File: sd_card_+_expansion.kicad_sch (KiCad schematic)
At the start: 1 part, among them J4 Micro_SD_Card_Det1

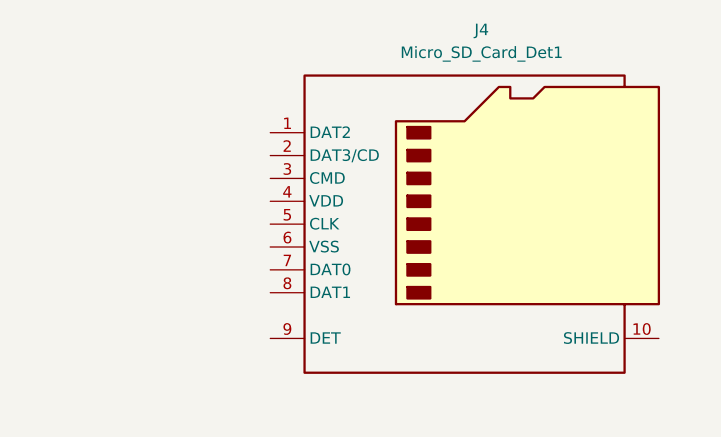
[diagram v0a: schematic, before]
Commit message: Added connectors
Added GPS and SD card connections
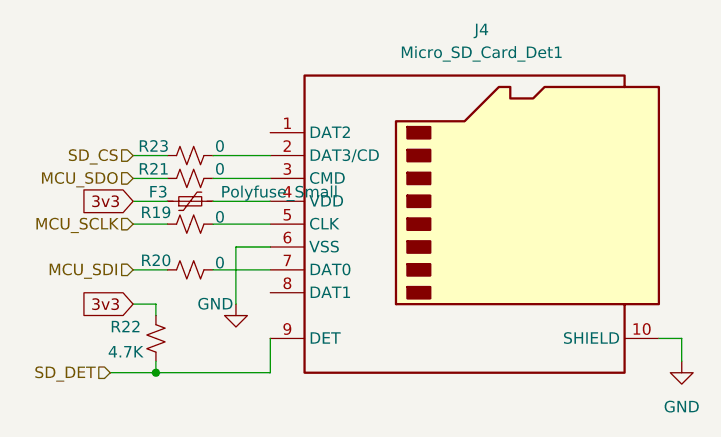
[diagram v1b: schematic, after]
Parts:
- added F3: Polyfuse_Small, symbol Device:Polyfuse_Small
- added R19, R20, R21, R23: 0, symbol Device:R_Small_US
- added R22: 4.7K, symbol Device:R_Small_US
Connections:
- net GND: now reaches J4.10 (SHIELD)
- net GND: now also J4.6 (VSS)
- net at J4.2 (DAT3/CD): now also R23.2
- net at J4.3 (CMD): now also R21.2
- net at J4.4 (VDD): now also F3.2
- net at J4.5 (CLK): now also R19.2
- net at J4.7 (DAT0): now also R20.2
- net SD_DET: now reaches J4.9 (DET)
- net SD_DET: now also R22.2
- new net 3v3: F3.1, R22.1
- new net MCU_SCLK: R19.1
- new net MCU_SDI: R20.1
- new net MCU_SDO: R21.1
- new net SD_CS: R23.1

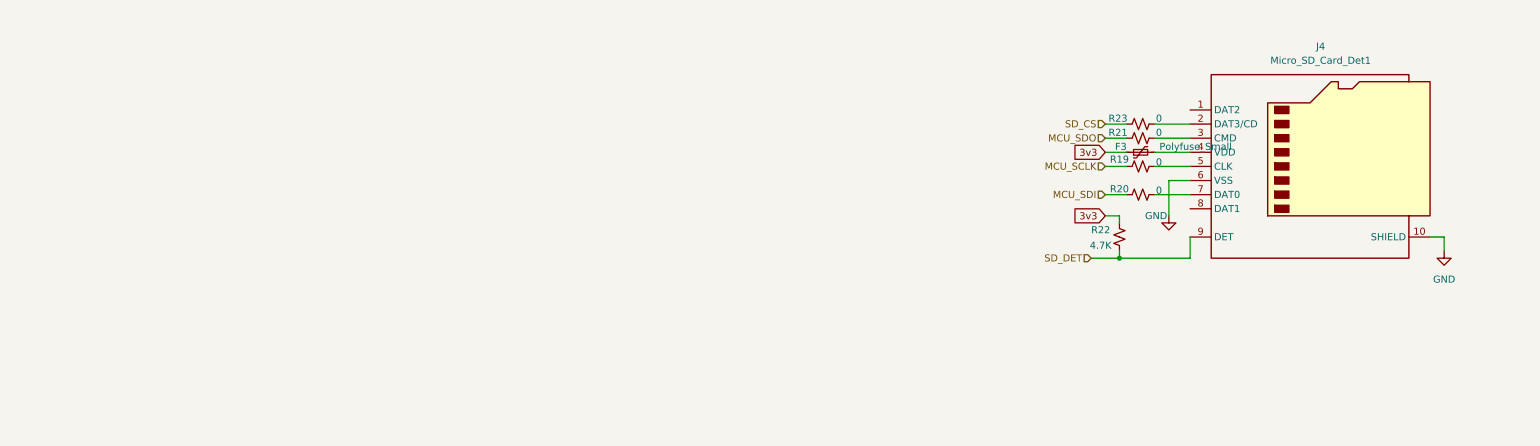
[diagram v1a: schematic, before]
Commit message: Updated schematics
Added the input current sense, expansion header and various test points.
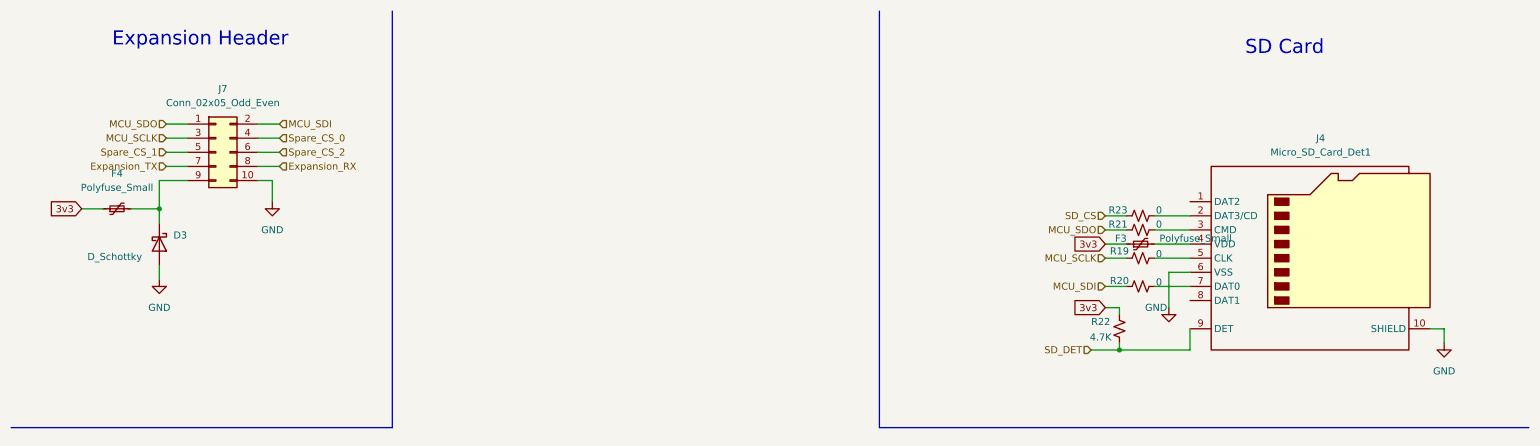
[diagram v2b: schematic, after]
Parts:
- added D3: D_Schottky, symbol Device:D_Schottky
- added F4: Polyfuse_Small, symbol Device:Polyfuse_Small
- added J7: Conn_02x05_Odd_Even, symbol Connector_Generic:Conn_02x05_Odd_Even
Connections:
- net 3v3: now also F4.1
- net GND: now also D3.2 (A), J7.10 (Pin_10)
- net MCU_SCLK: now also J7.3 (Pin_3)
- net MCU_SDI: now also J7.2 (Pin_2)
- net MCU_SDO: now also J7.1 (Pin_1)
- new net: D3.1 (K), F4.2, J7.9 (Pin_9)
- new net Expansion_RX: J7.8 (Pin_8)
- new net Expansion_TX: J7.7 (Pin_7)
- new net Spare_CS_0: J7.4 (Pin_4)
- new net Spare_CS_1: J7.5 (Pin_5)
- new net Spare_CS_2: J7.6 (Pin_6)
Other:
- note added: "Expansion Header"
- note added: "SD Card"
- moved on the sheet: F3, J4, R19, R20, R21, R22, R23

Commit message: Added RPI stuff
Added power passives and usb passives
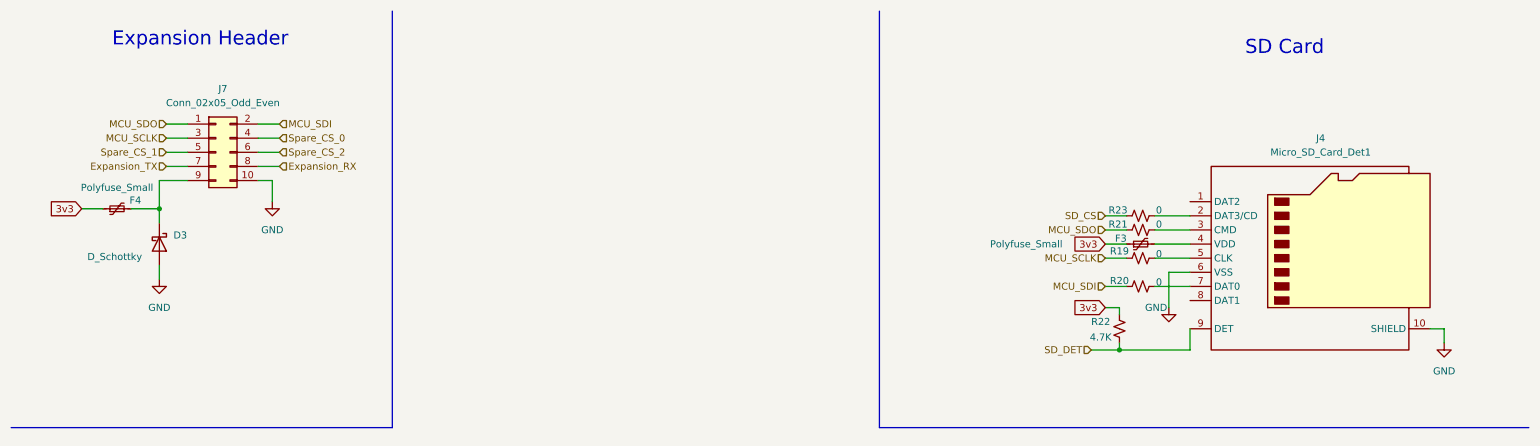
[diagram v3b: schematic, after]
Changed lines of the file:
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@@
 		(on_board yes)
 		(dnp no)
-		(fields_autoplaced yes)
 		(property "Reference" "F4"
-			(at 30.48 41.91 90)
+			(at 33.782 46.736 90)
 			(effects
 				(font
@@
 		)
 		(property "Value" "Polyfuse_Small"
-			(at 224.536 53.594 90)
+			(at 194.056 54.61 90)
 			(effects
 				(font

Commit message: Setup top sheet
Added TVS diodes, updated top sheet, misc label fixes
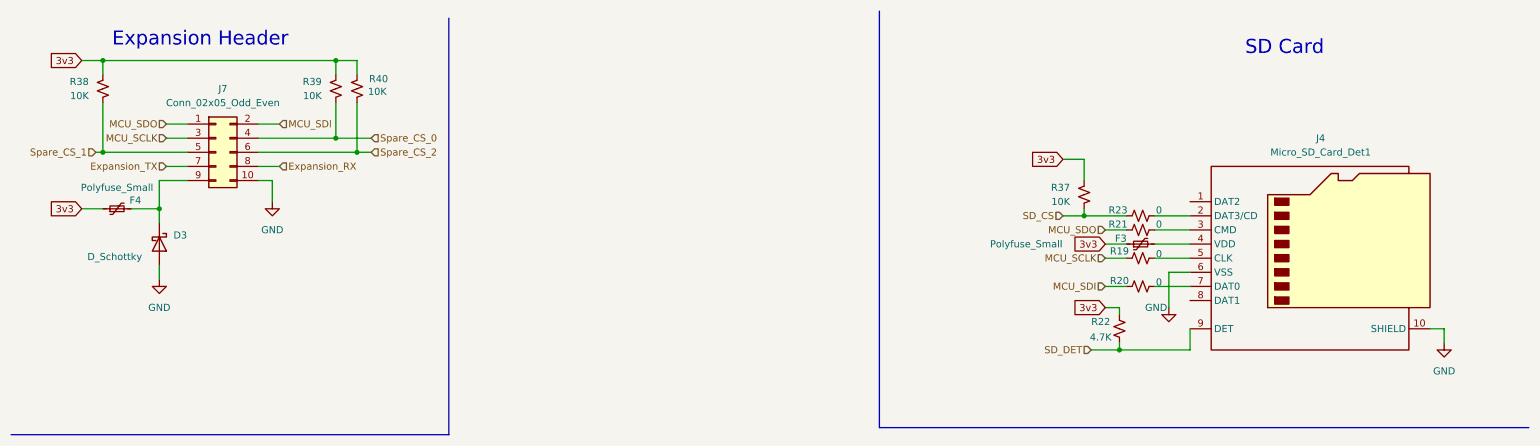
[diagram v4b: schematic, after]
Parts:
- added R37, R38, R39, R40: 10K, symbol Device:R_Small_US
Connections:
- net 3v3: now also R37.1, R38.1, R39.1, R40.1
- net SD_CS: now also R37.2
- net Spare_CS_0: now also R39.2
- net Spare_CS_1: now also R38.2
- net Spare_CS_2: now also R40.2

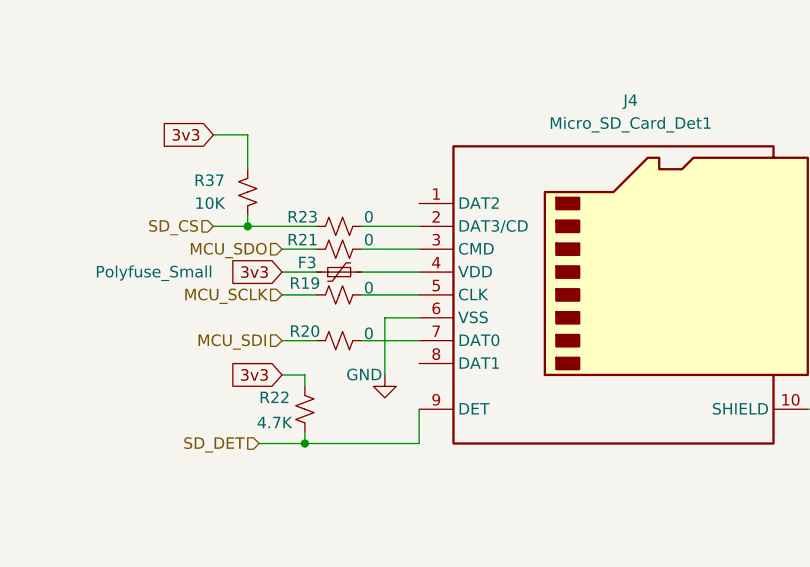
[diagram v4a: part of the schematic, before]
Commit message: Updated sheet to sheet pinout
Updated pinouts and cleared ERCs
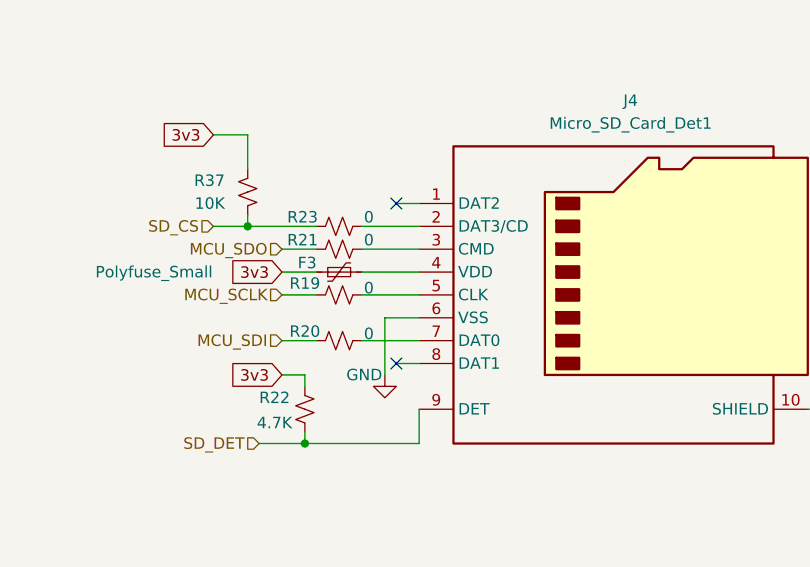
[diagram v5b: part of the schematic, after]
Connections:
- no-connect marks 0 -> 2
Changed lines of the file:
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@@
 		(color 0 0 0 0)
+	)
+	(no_connect
+		(at 220.98 64.77)
+	)
+	(no_connect
+		(at 220.98 46.99)
 	)
 	(wire
 		(pts
 			(xy 208.28 52.07) (xy 212.09 52.07)
+		)
+		(stroke
+			(width 0)
+			(type default)
+		)
+	)
+	(wire
+		(pts
+			(xy 220.98 64.77) (xy 223.52 64.77)
 		)
 		(stroke
@@
 		)
 		(stroke
+			(width 0)
+			(type default)
+		)
+	)
+	(wire
+		(pts
+			(xy 220.98 46.99) (xy 223.52 46.99)
+		)
+		(stroke

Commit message: started layout
Preliminary footprint selection
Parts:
- D3: footprint (none) -> Diode_SMD:D_SOD-123
- F3, F4: footprint (none) -> Fuse:Fuse_1206_3216Metric
- J4: footprint (none) -> Connector_Card:microSD_HC_Hirose_DM3D-SF
- J7: footprint (none) -> Connector_PinHeader_2.54mm:PinHeader_2x05_P2.54mm_Vertical
- R19, R20, R21, R22, R23, R37, R38, R39, R40: footprint (none) -> Resistor_SMD:R_0603_1608Metric
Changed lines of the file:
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@@
 			)
 		)
-		(property "Footprint" ""
+		(property "Footprint" "Connector_Card:microSD_HC_Hirose_DM3D-SF"
 			(at 298.45 39.37 0)
 			(effects
@@
 			)
 		)
-		(property "Footprint" ""
+		(property "Footprint" "Resistor_SMD:R_0603_1608Metric"
 			(at 210.82 69.85 0)
 			(effects
@@
 			)
 		)
-		(property "Footprint" ""
+		(property "Footprint" "Resistor_SMD:R_0603_1608Metric"
 			(at 214.63 62.23 0)
 			(effects
@@
 			)
 		)
-		(property "Footprint" ""
+		(property "Footprint" "Diode_SMD:D_SOD-123"
 			(at 38.1 54.61 0)
 			(effects
@@
 			)
 		)
-		(property "Footprint" ""
+		(property "Footprint" "Resistor_SMD:R_0603_1608Metric"
 			(at 214.63 49.53 0)
 			(effects
@@
 			)
 		)
-		(property "Footprint" ""
+		(property "Footprint" "Resistor_SMD:R_0603_1608Metric"
 			(at 73.66 26.67 0)
 			(effects
@@
 			)
 		)
-		(property "Footprint" ""
+		(property "Footprint" "Fuse:Fuse_1206_3216Metric"
 			(at 35.56 46.99 0)
 			(effects
@@
 			)
 		)
-		(property "Footprint" ""
+		(property "Footprint" "Fuse:Fuse_1206_3216Metric"
 			(at 219.71 53.34 0)
 			(effects
@@
 			)
 		)
-		(property "Footprint" ""
+		(property "Footprint" "Resistor_SMD:R_0603_1608Metric"
 			(at 214.63 52.07 0)
 			(effects
@@
 			)
 		)
-		(property "Footprint" ""
+		(property "Footprint" "Resistor_SMD:R_0603_1608Metric"
 			(at 69.85 26.67 0)
 			(effects
@@
 			)
 		)
-		(property "Footprint" ""
+		(property "Footprint" "Resistor_SMD:R_0603_1608Metric"
 			(at 27.94 26.67 0)
 			(effects
@@
 			)
 		)
-		(property "Footprint" ""
+		(property "Footprint" "Resistor_SMD:R_0603_1608Metric"
 			(at 214.63 57.15 0)
 			(effects
@@
 			)
 		)
-		(property "Footprint" ""
+		(property "Footprint" "Connector_PinHeader_2.54mm:PinHeader_2x05_P2.54mm_Vertical"
 			(at 48.26 38.1 0)
 			(effects
@@
 			)
 		)
-		(property "Footprint" ""
+		(property "Footprint" "Resistor_SMD:R_0603_1608Metric"
 			(at 204.47 45.72 0)
 			(effects

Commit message: footprint cleanup
switched to 0402 resistors, updated connectors, etc...
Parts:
- R19, R20, R21, R22, R23, R37, R38, R39, R40: footprint Resistor_SMD:R_0603_1608Metric -> Resistor_SMD:R_0402_1005Metric
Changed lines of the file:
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@@
 			)
 		)
-		(property "Footprint" "Resistor_SMD:R_0603_1608Metric"
+		(property "Footprint" "Resistor_SMD:R_0402_1005Metric"
 			(at 210.82 69.85 0)
 			(effects
@@
 			)
 		)
-		(property "Footprint" "Resistor_SMD:R_0603_1608Metric"
+		(property "Footprint" "Resistor_SMD:R_0402_1005Metric"
 			(at 214.63 62.23 0)
 			(effects
@@
 			)
 		)
-		(property "Footprint" "Resistor_SMD:R_0603_1608Metric"
+		(property "Footprint" "Resistor_SMD:R_0402_1005Metric"
 			(at 214.63 49.53 0)
 			(effects
@@
 			)
 		)
-		(property "Footprint" "Resistor_SMD:R_0603_1608Metric"
+		(property "Footprint" "Resistor_SMD:R_0402_1005Metric"
 			(at 73.66 26.67 0)
 			(effects
@@
 			)
 		)
-		(property "Footprint" "Resistor_SMD:R_0603_1608Metric"
+		(property "Footprint" "Resistor_SMD:R_0402_1005Metric"
 			(at 214.63 52.07 0)
 			(effects
@@
 			)
 		)
-		(property "Footprint" "Resistor_SMD:R_0603_1608Metric"
+		(property "Footprint" "Resistor_SMD:R_0402_1005Metric"
 			(at 69.85 26.67 0)
 			(effects
@@
 			)
 		)
-		(property "Footprint" "Resistor_SMD:R_0603_1608Metric"
+		(property "Footprint" "Resistor_SMD:R_0402_1005Metric"
 			(at 27.94 26.67 0)
 			(effects
@@
 			)
 		)
-		(property "Footprint" "Resistor_SMD:R_0603_1608Metric"
+		(property "Footprint" "Resistor_SMD:R_0402_1005Metric"
 			(at 214.63 57.15 0)
 			(effects
@@
 			)
 		)
-		(property "Footprint" "Resistor_SMD:R_0603_1608Metric"
+		(property "Footprint" "Resistor_SMD:R_0402_1005Metric"
 			(at 204.47 45.72 0)
 			(effects

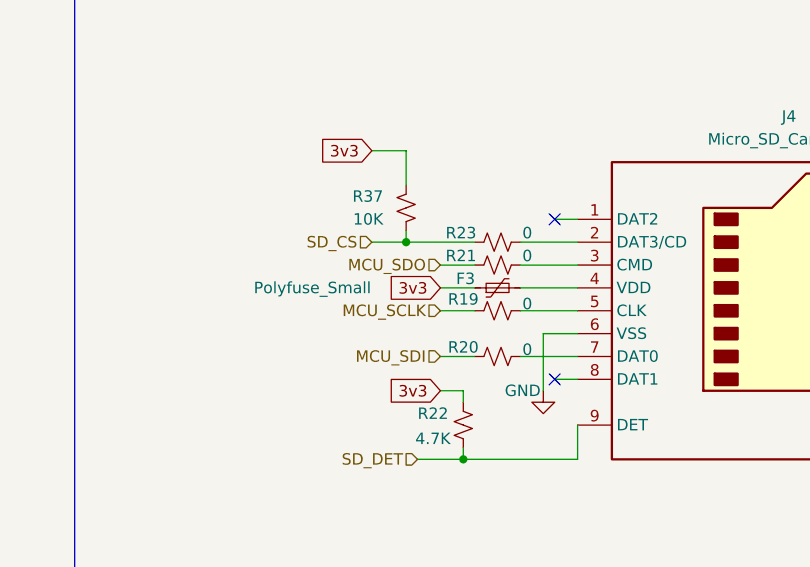
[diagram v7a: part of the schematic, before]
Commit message: Distributed caps
Remembered to add decoupling caps
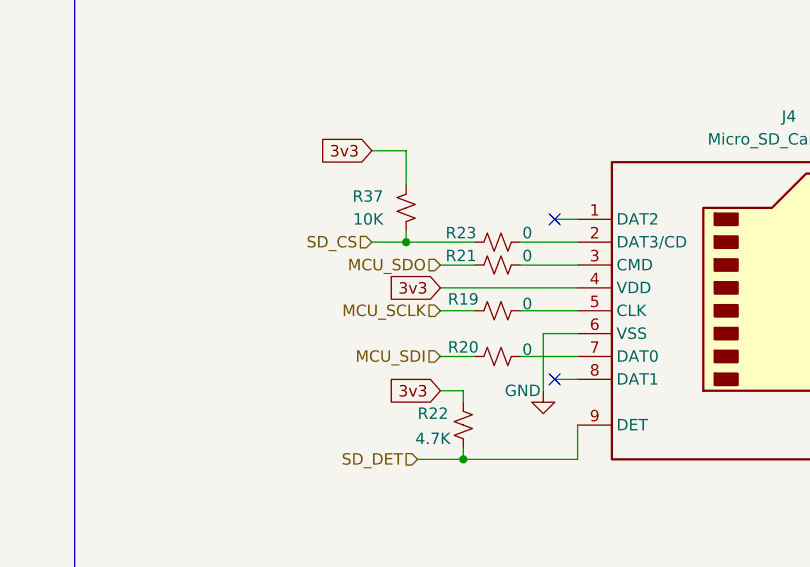
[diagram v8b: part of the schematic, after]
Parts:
- removed F3: Polyfuse_Small, Fuse:Fuse_1206_3216Metric, symbol Device:Polyfuse_Small
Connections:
- net 3v3: now also J4.4 (VDD)
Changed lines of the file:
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@@
 	(wire
 		(pts
-			(xy 208.28 54.61) (xy 212.09 54.61)
+			(xy 208.28 54.61) (xy 223.52 54.61)
 		)
 		(stroke
@@
 		(pts
 			(xy 39.37 33.02) (xy 43.18 33.02)
-		)
-		(stroke
-			(width 0)
-			(type default)
-		)
-	)
-	(wire
-		(pts
-			(xy 217.17 54.61) (xy 223.52 54.61)
 		)
 		(stroke
@@
 					(unit 1)
 				)
-			)
-		)
-	)
-	(symbol
-		(lib_id "Device:Polyfuse_Small")
-		(at 214.63 54.61 90)
-		(unit 1)
-		(exclude_from_sim no)
-		(in_bom yes)
-		(on_board yes)
-		(dnp no)
-		(property "Reference" "F3"
-			(at 211.074 53.594 90)
-			(effects
-				(font
-					(size 1.27 1.27)
-				)
-			)
-		)
-		(property "Value" "Polyfuse_Small"
-			(at 194.056 54.61 90)
-			(effects
-				(font
-					(size 1.27 1.27)
-				)
-			)
-		)
-		(property "Footprint" "Fuse:Fuse_1206_3216Metric"
-			(at 219.71 53.34 0)
-			(effects
-				(font
-					(size 1.27 1.27)
-				)
-				(justify left)
-				(hide yes)
-			)
-		)
-		(property "Datasheet" "~"
-			(at 214.63 54.61 0)
-			(effects
-				(font
-					(size 1.27 1.27)
-				)
-				(hide yes)
-			)
-		)
-		(property "Description" "Resettable fuse, polymeric positive temperature coefficient, small symbol"
-			(at 214.63 54.61 0)
-			(effects
-				(font
-					(size 1.27 1.27)
-				)
-				(hide yes)
-			)
-		)
-		(pin "2"
-		)
-		(pin "1"
-		)
-		(instances
-			(project "moon_child"
-				(path "/9fe08eae-9310-46cf-b272-eac4209a7b3e/68da5adc-0b2d-4a3d-9dbd-3c9825249f40"
-					(reference "F3")
-					(unit 1)
-				)
